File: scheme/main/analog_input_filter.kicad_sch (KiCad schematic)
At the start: 10 parts, among them U29 RS8551

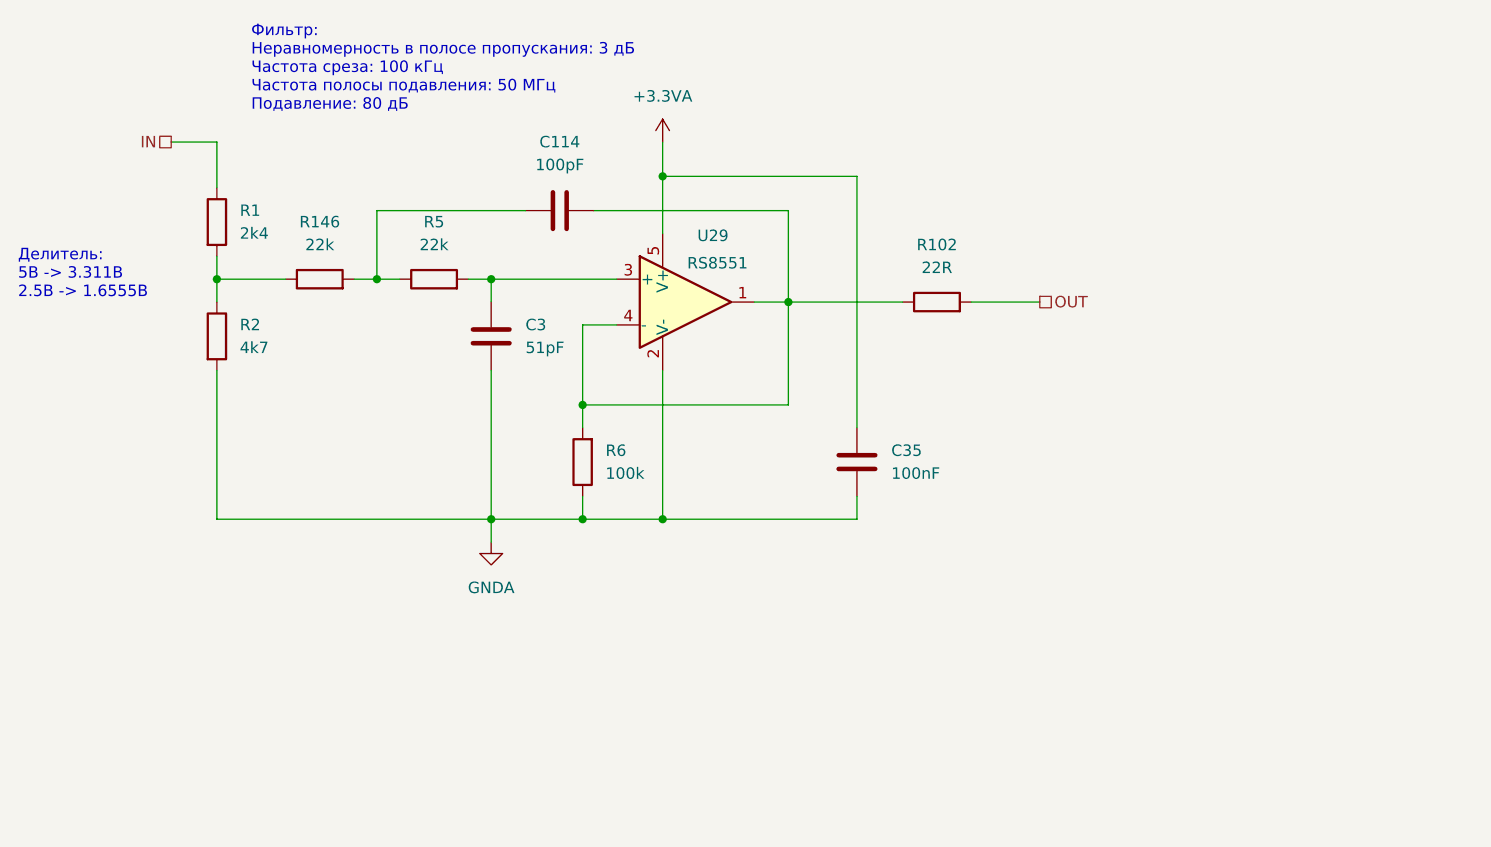
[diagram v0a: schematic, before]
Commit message: added analog input 0 && sheets sort
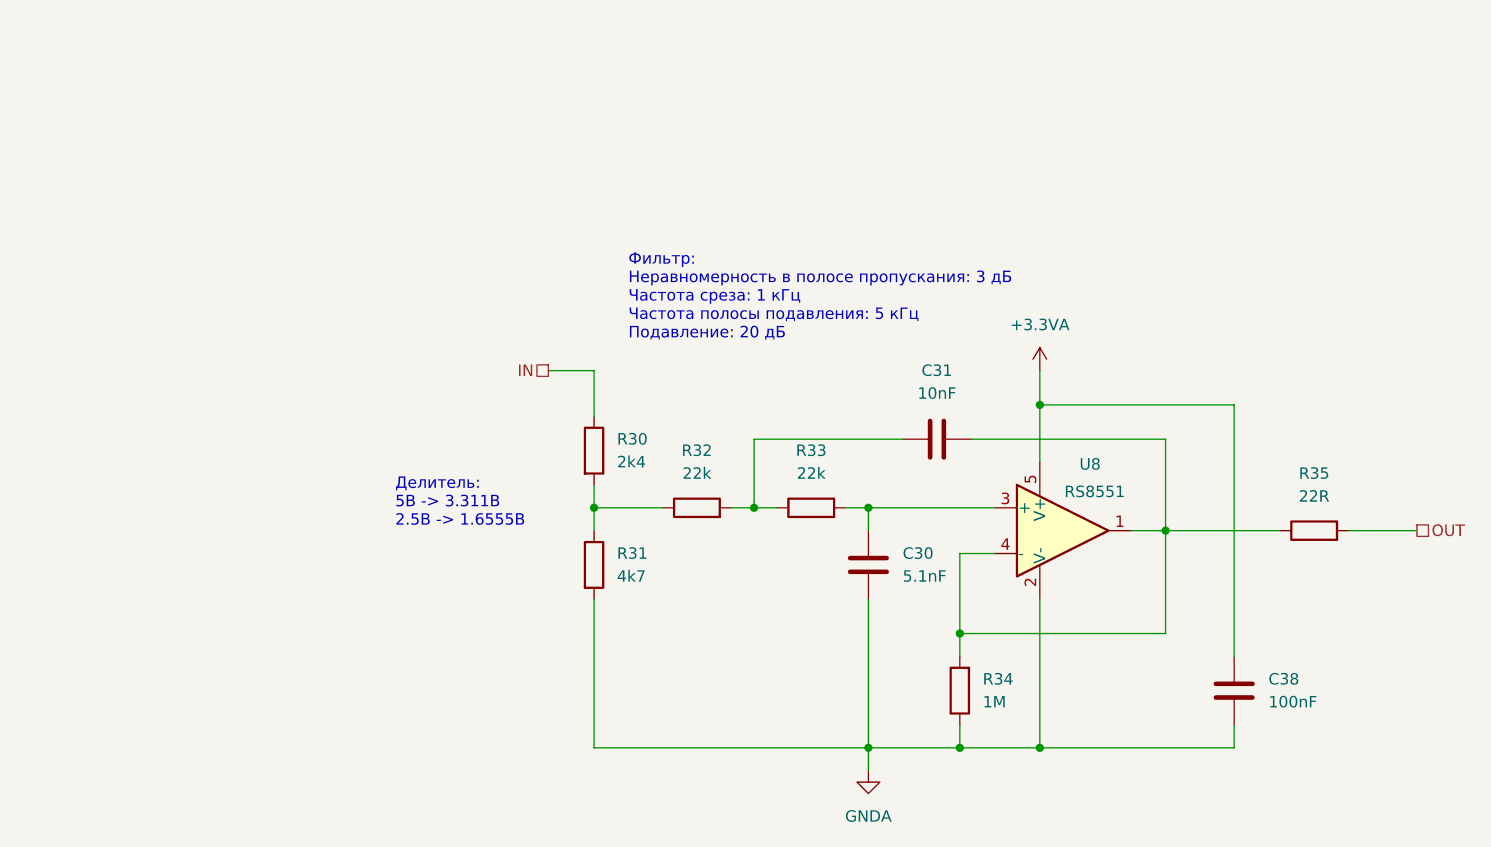
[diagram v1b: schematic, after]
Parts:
- removed C114: 100pF, Capacitor_SMD:C_0805_2012Metric, symbol Device:C
- removed C3: 51pF, Capacitor_SMD:C_0805_2012Metric, symbol Device:C
- removed C35: 100nF, Capacitor_SMD:C_0805_2012Metric, symbol Device:C
- removed R1: 2k4, Resistor_SMD:R_0805_2012Metric, symbol Device:R
- removed R102: 22R, Resistor_SMD:R_0805_2012Metric, symbol Device:R
- removed R146, R5: 22k, Resistor_SMD:R_0805_2012Metric, symbol Device:R
- removed R2: 4k7, Resistor_SMD:R_0805_2012Metric, symbol Device:R
- removed R6: 100k, Resistor_SMD:R_0805_2012Metric, symbol Device:R
- removed U29: RS8551, Package_TO_SOT_SMD:TSOT-23-5, symbol main:RS8551
- added C30: 5.1nF, Capacitor_SMD:C_0805_2012Metric, symbol Device:C
- added C31: 10nF, Capacitor_SMD:C_0805_2012Metric, symbol Device:C
- added C38: 100nF, Capacitor_SMD:C_0805_2012Metric, symbol Device:C
- added R30: 2k4, Resistor_SMD:R_0805_2012Metric, symbol Device:R
- added R31: 4k7, Resistor_SMD:R_0805_2012Metric, symbol Device:R
- added R32, R33: 22k, Resistor_SMD:R_0805_2012Metric, symbol Device:R
- added R34: 1M, Resistor_SMD:R_0805_2012Metric, symbol Device:R
- added R35: 22R, Resistor_SMD:R_0805_2012Metric, symbol Device:R
- added U8: RS8551, Package_TO_SOT_SMD:TSOT-23-5, symbol main:RS8551
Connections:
- net +3.3VA: now also C38.1, U8.5 (V+)
- net GNDA: now also C30.2, C38.2, R31.2, R34.1, U8.2 (V-)
- net IN: now also R30.1
- net OUT: now also R35.2
- new net: C30.1, R33.2, U8.3 (+)
- new net: R30.2, R31.1, R32.1
- new net: C31.2, R32.2, R33.1
- new net: C31.1, R34.2, R35.1, U8.1, U8.4 (-)
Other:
- note added: "Фильтр: Неравномерность в полосе пропускания: 3 дБ Частота среза: 1 кГц Частота полосы подавления: 5 кГц Подавление: 20 дБ"
- note removed: "Фильтр: Неравномерность в полосе пропускания: 3 дБ Частота среза: 100 кГц Частота полосы подавления: 50 МГц Подавление: 80 дБ"
- title: Фильтр тока -> (none)
